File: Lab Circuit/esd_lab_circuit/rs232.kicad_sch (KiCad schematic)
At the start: 8 parts, among them U4 RS232, U7 MAX232

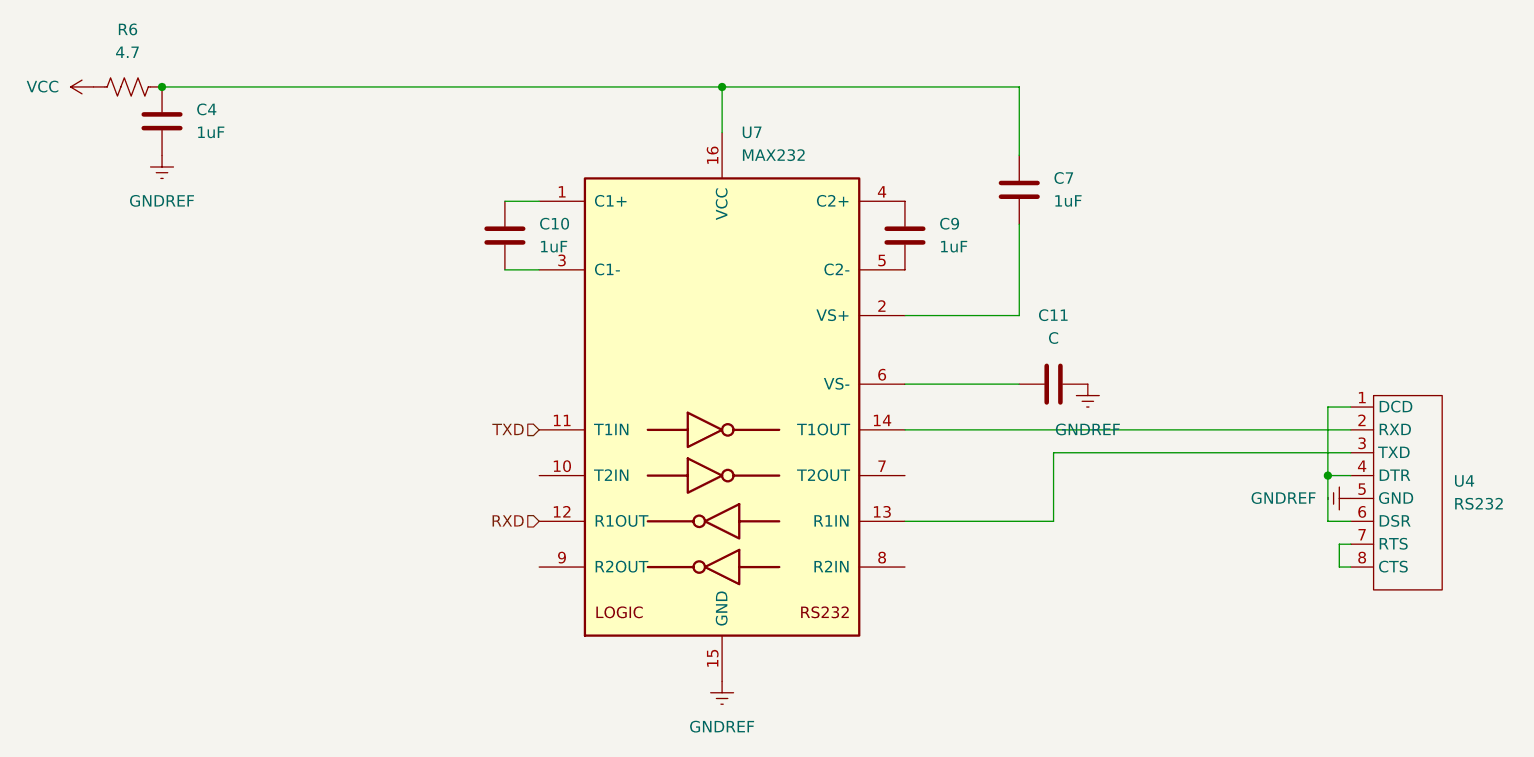
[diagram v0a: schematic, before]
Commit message: Added Debug Latch to schematic
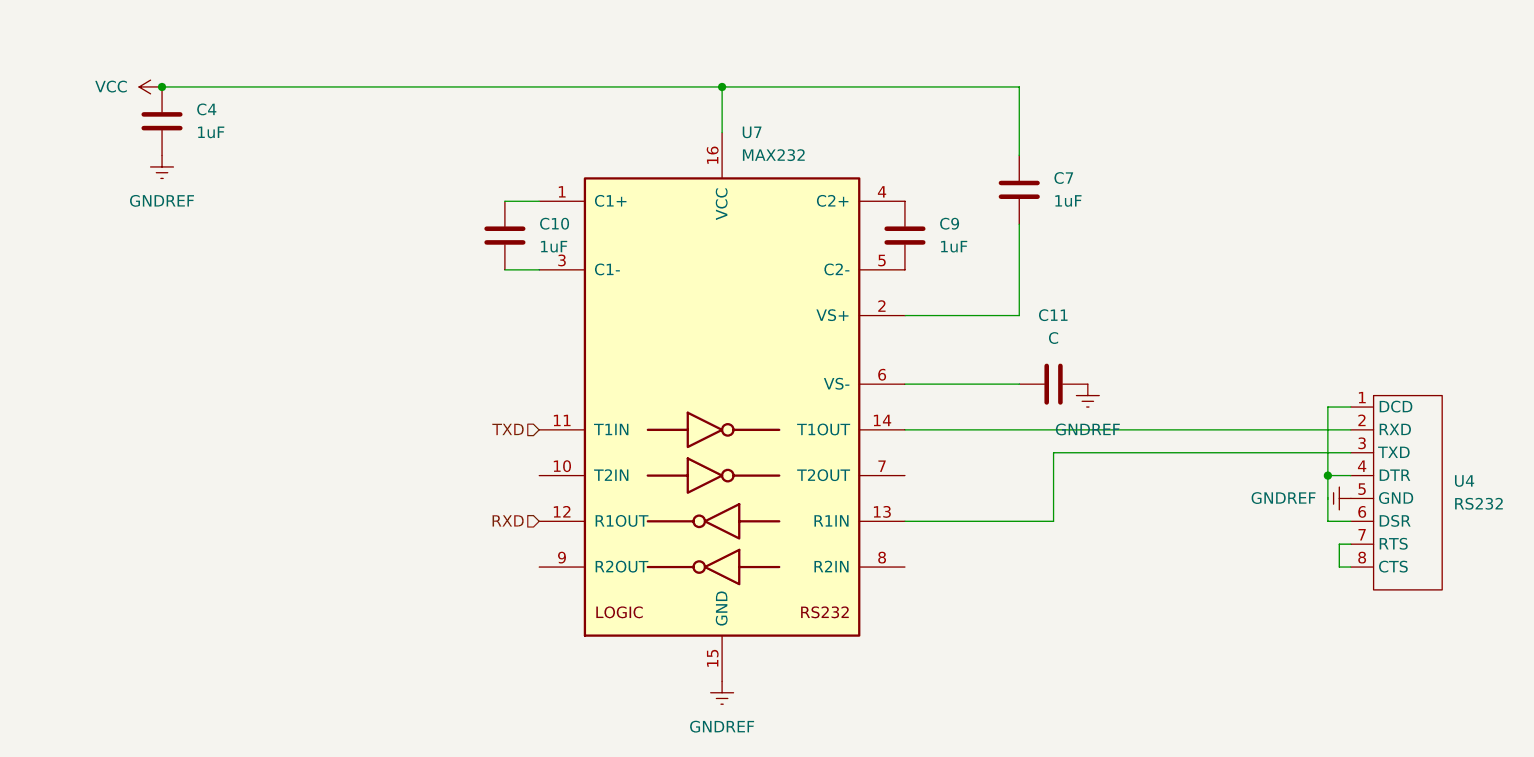
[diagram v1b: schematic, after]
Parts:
- removed R6: 4.7, symbol Device:R_US
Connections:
- net VCC: now also C4.1, C7.1, U7.16 (VCC)
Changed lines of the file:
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@@
-	(wire
-		(pts
-			(xy 187.96 80.01) (xy 187.96 87.63)
-		)
-		(stroke
-			(width 0)
-			(type default)
-		)
-	)
 	(wire
 		(pts
@@
 	(wire
 		(pts
-			(xy 190.5 80.01) (xy 187.96 80.01)
+			(xy 187.96 80.01) (xy 190.5 80.01)
 		)
 		(stroke
@@
 		(pts
 			(xy 153.67 77.47) (xy 140.97 77.47)
+		)
+		(stroke
+			(width 0)
+			(type default)
+		)
+	)
+	(wire
+		(pts
+			(xy 187.96 87.63) (xy 187.96 80.01)
 		)
 		(stroke
@@
 	(symbol
 		(lib_id "power:VCC")
-		(at 50.8 44.45 90)
+		(at 58.42 44.45 90)
 		(unit 1)
 		(exclude_from_sim no)
@@
 		(fields_autoplaced yes)
 		(property "Reference" "#PWR023"
-			(at 54.61 44.45 0)
+			(at 62.23 44.45 0)
 			(effects
 				(font
@@
 		)
 		(property "Value" "VCC"
-			(at 46.99 44.4499 90)
+			(at 54.61 44.4499 90)
 			(effects
 				(font
@@
 		)
 		(property "Footprint" ""
-			(at 50.8 44.45 0)
+			(at 58.42 44.45 0)
 			(effects
 				(font
@@
 		)
 		(property "Datasheet" ""
-			(at 50.8 44.45 0)
+			(at 58.42 44.45 0)
 			(effects
 				(font
@@
 		)
 		(property "Description" "Power symbol creates a global label with name \"VCC\""
-			(at 50.8 44.45 0)
+			(at 58.42 44.45 0)
 			(effects
 				(font
@@
 					(unit 1)
 				)
-			)
-		)
-	)
-	(symbol
-		(lib_id "Device:R_US")
-		(at 54.61 44.45 270)
-		(unit 1)
-		(exclude_from_sim no)
-		(in_bom yes)
-		(on_board yes)
-		(dnp no)
-		(fields_autoplaced yes)
-		(property "Reference" "R6"
-			(at 54.61 38.1 90)
-			(effects
-				(font
-					(size 1.27 1.27)
-				)
-			)
-		)
-		(property "Value" "4.7"
-			(at 54.61 40.64 90)
-			(effects
-				(font
-					(size 1.27 1.27)
-				)
-			)
-		)
-		(property "Footprint" ""
-			(at 54.356 45.466 90)
-			(effects
-				(font
-					(size 1.27 1.27)
-				)
-				(hide yes)
-			)
-		)
-		(property "Datasheet" "~"
-			(at 54.61 44.45 0)
-			(effects
-				(font
-					(size 1.27 1.27)
-				)
-				(hide yes)
-			)
-		)
-		(property "Description" "Resistor, US symbol"
-			(at 54.61 44.45 0)
-			(effects
-				(font
-					(size 1.27 1.27)
-				)
-				(hide yes)
-			)
-		)
-		(pin "2"
-		)
-		(pin "1"
-		)
-		(instances
-			(project ""
-				(path "/e737370b-dddd-4d85-b455-d3366cc4c4a7/8702a0d8-b2bf-4523-b629-ab6ae5152baf"
-					(reference "R6")
-					(unit 1)
-				)
